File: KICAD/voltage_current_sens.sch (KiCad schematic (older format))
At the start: 17 parts, among them Q4 BC847, Q5 BC847, U8 LT6016, U9 AD8030

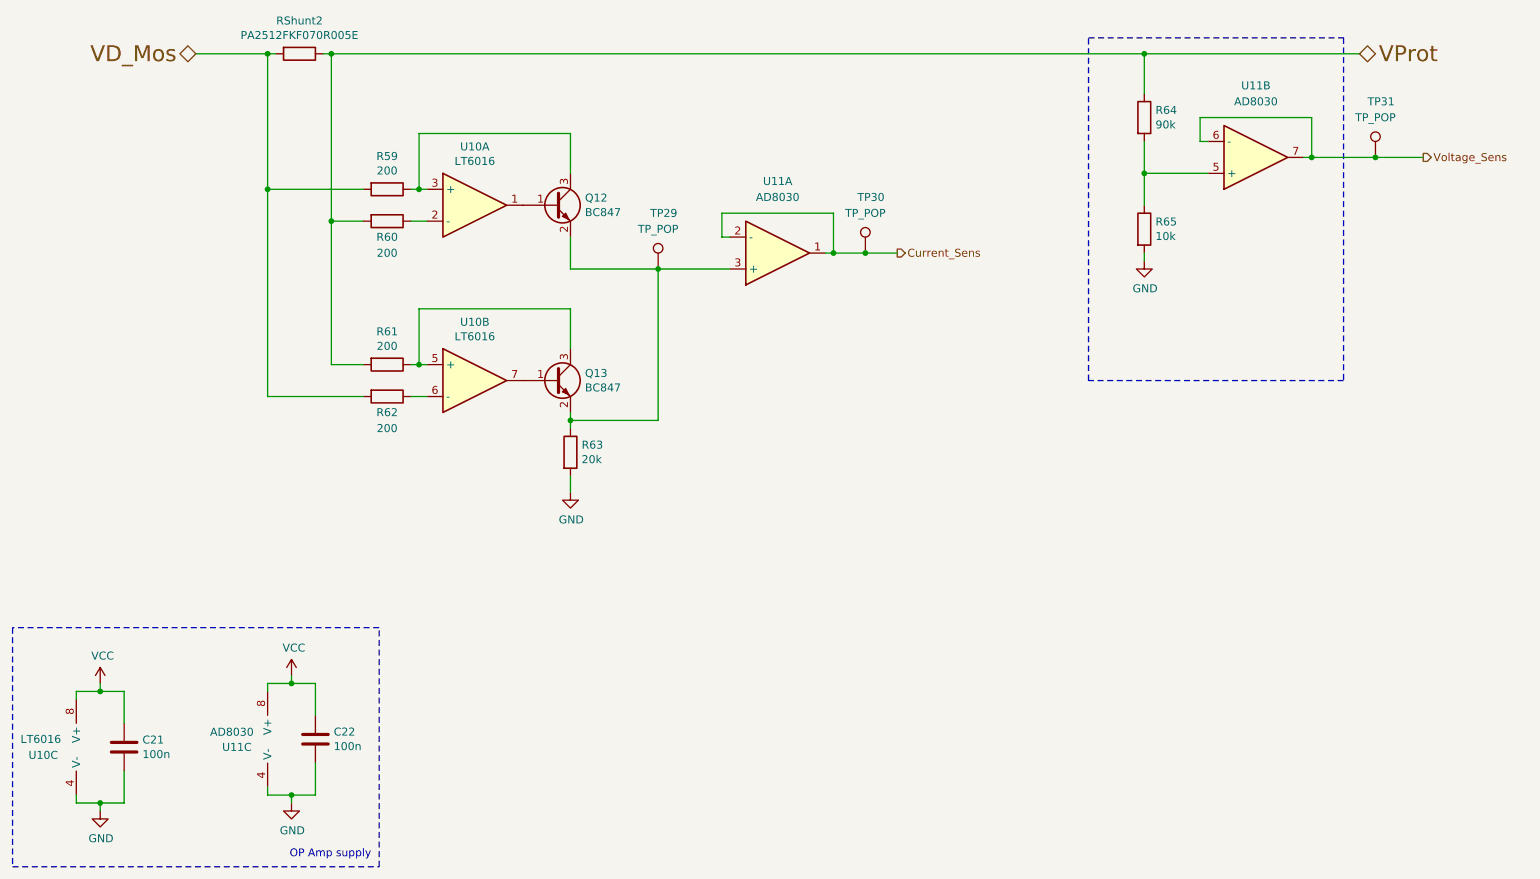
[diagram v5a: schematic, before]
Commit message: mod. ref rail on kicad
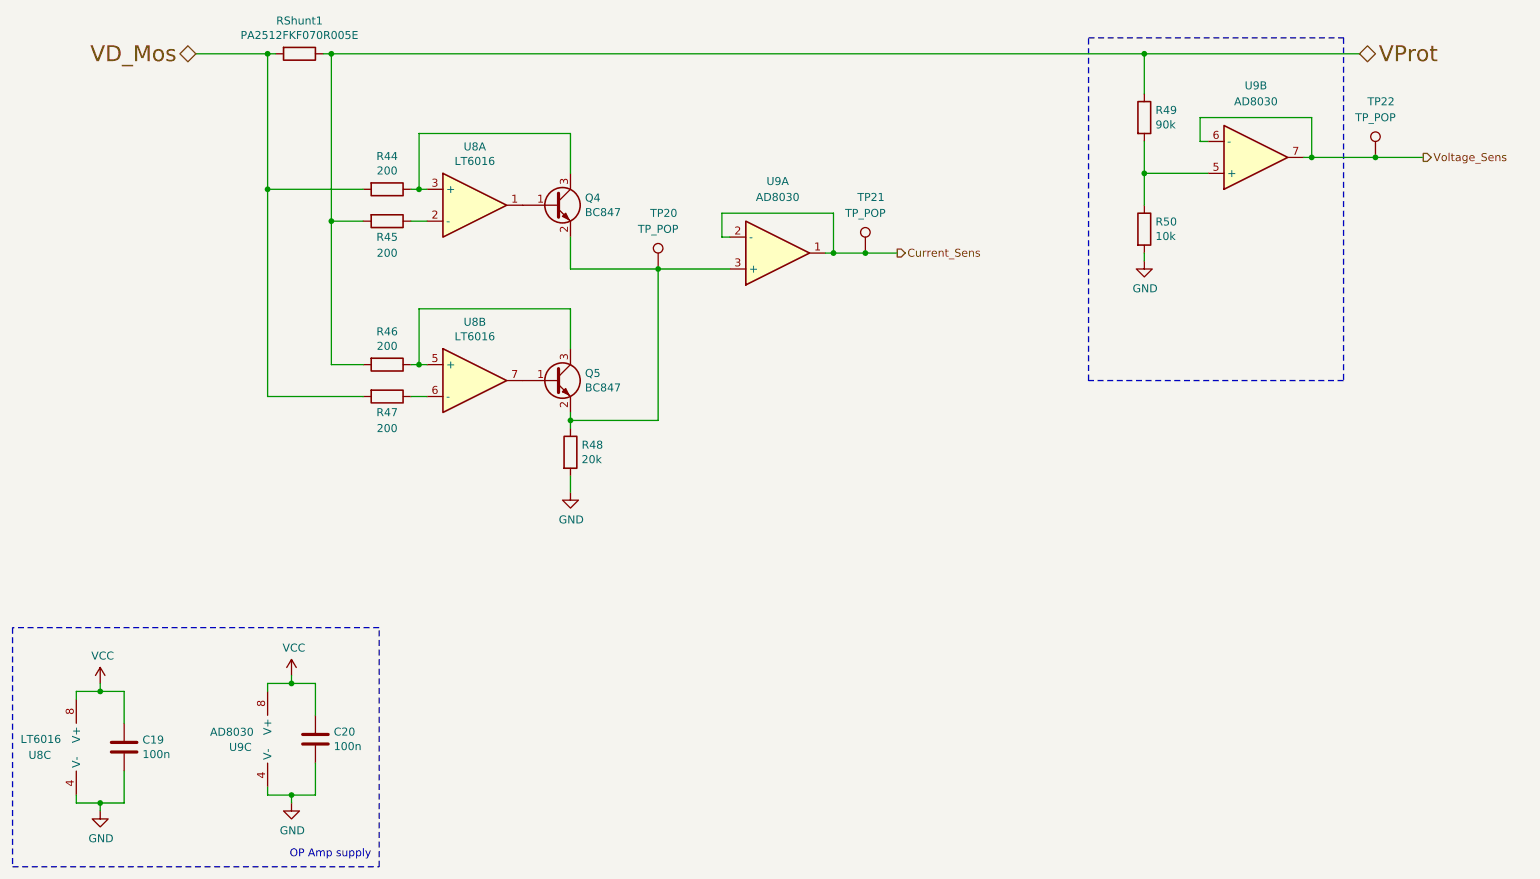
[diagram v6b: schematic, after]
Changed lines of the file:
@@
 AR Path="/60F19D5B/6109114F" Ref="RShunt2"  Part="1"
 AR Path="/60F171CE/6109114F" Ref="RShunt1"  Part="1"
-F 0 "RShunt2" V 2143 2600 50  0000 C CNN
+F 0 "RShunt1" V 2143 2600 50  0000 C CNN
 F 1 "PA2512FKF070R005E" V 2234 2600 50  0000 C CNN
 F 2 "Resistor_SMD:R_2512_6332Metric_Pad1.52x3.35mm_HandSolder" V 2280 2600 50  0001 C CNN
@@
 AR Path="/60F19D5B/61091B7C" Ref="R60"  Part="1"
 AR Path="/60F171CE/61091B7C" Ref="R45"  Part="1"
-F 0 "R60" V 3000 3650 50  0000 C CNN
+F 0 "R45" V 3000 3650 50  0000 C CNN
 F 1 "200" V 3100 3650 50  0000 C CNN
 F 2 "Sesame_footprint:R_0805_2012Metric_Pad1.20x1.40mm_HandSolder" V 2830 3650 50  0001 C CNN
@@
 AR Path="/60F19D5B/610923D6" Ref="R59"  Part="1"
 AR Path="/60F171CE/610923D6" Ref="R44"  Part="1"
-F 0 "R59" V 2693 3450 50  0000 C CNN
+F 0 "R44" V 2693 3450 50  0000 C CNN
 F 1 "200" V 2784 3450 50  0000 C CNN
 F 2 "Sesame_footprint:R_0805_2012Metric_Pad1.20x1.40mm_HandSolder" V 2830 3450 50  0001 C CNN
@@
 AR Path="/60F171CE/610DEA27" Ref="#PWR068"  Part="1"
 AR Path="/60F19D5B/610DEA27" Ref="#PWR080"  Part="1"
-F 0 "#PWR080" H 7650 3650 50  0001 C CNN
+F 0 "#PWR068" H 7650 3650 50  0001 C CNN
 F 1 "GND" H 7655 3727 50  0000 C CNN
 F 2 "" H 7650 3900 50  0001 C CNN
@@
 AR Path="/60F171CE/610DC636" Ref="R50"  Part="1"
 AR Path="/60F19D5B/610DC636" Ref="R65"  Part="1"
-F 0 "R65" H 7720 3746 50  0000 L CNN
+F 0 "R50" H 7720 3746 50  0000 L CNN
 F 1 "10k" H 7720 3655 50  0000 L CNN
 F 2 "Sesame_footprint:R_0805_2012Metric_Pad1.20x1.40mm_HandSolder" V 7580 3700 50  0001 C CNN
@@
 AR Path="/60F171CE/610DBB97" Ref="R49"  Part="1"
 AR Path="/60F19D5B/610DBB97" Ref="R64"  Part="1"
-F 0 "R64" H 7720 3046 50  0000 L CNN
+F 0 "R49" H 7720 3046 50  0000 L CNN
 F 1 "90k" H 7720 2955 50  0000 L CNN
 F 2 "Sesame_footprint:R_0805_2012Metric_Pad1.20x1.40mm_HandSolder" V 7580 3000 50  0001 C CNN
@@
 AR Path="/60F171CE/61382079" Ref="Q4"  Part="1"
 AR Path="/60F19D5B/61382079" Ref="Q12"  Part="1"
-F 0 "Q12" H 4141 3596 50  0000 L CNN
+F 0 "Q4" H 4141 3596 50  0000 L CNN
 F 1 "BC847" H 4141 3505 50  0000 L CNN
 F 2 "Package_TO_SOT_SMD:SOT-23" H 4150 3475 50  0001 L CIN
@@
 AR Path="/60F171CE/613844DA" Ref="Q5"  Part="1"
 AR Path="/60F19D5B/613844DA" Ref="Q13"  Part="1"
-F 0 "Q13" H 4141 4696 50  0000 L CNN
+F 0 "Q5" H 4141 4696 50  0000 L CNN
 F 1 "BC847" H 4141 4605 50  0000 L CNN
 F 2 "Package_TO_SOT_SMD:SOT-23" H 4150 4575 50  0001 L CIN
@@
 AR Path="/60F171CE/6138CEF9" Ref="R48"  Part="1"
 AR Path="/60F19D5B/6138CEF9" Ref="R63"  Part="1"
-F 0 "R63" H 4120 5146 50  0000 L CNN
+F 0 "R48" H 4120 5146 50  0000 L CNN
 F 1 "20k" H 4120 5055 50  0000 L CNN
 F 2 "Sesame_footprint:R_0805_2012Metric_Pad1.20x1.40mm_HandSolder" V 3980 5100 50  0001 C CNN
@@
 AR Path="/60F171CE/61391300" Ref="#PWR067"  Part="1"
 AR Path="/60F19D5B/61391300" Ref="#PWR079"  Part="1"
-F 0 "#PWR079" H 4050 5100 50  0001 C CNN
+F 0 "#PWR067" H 4050 5100 50  0001 C CNN
 F 1 "GND" H 4055 5177 50  0000 C CNN
 F 2 "" H 4050 5350 50  0001 C CNN
@@
 AR Path="/60F19D5B/61397C3C" Ref="R61"  Part="1"
 AR Path="/60F171CE/61397C3C" Ref="R46"  Part="1"
-F 0 "R61" V 2693 4550 50  0000 C CNN
+F 0 "R46" V 2693 4550 50  0000 C CNN
 F 1 "200" V 2784 4550 50  0000 C CNN
 F 2 "Sesame_footprint:R_0805_2012Metric_Pad1.20x1.40mm_HandSolder" V 2830 4550 50  0001 C CNN
@@
 AR Path="/60F19D5B/61398F33" Ref="R62"  Part="1"
 AR Path="/60F171CE/61398F33" Ref="R47"  Part="1"
-F 0 "R62" V 3000 4750 50  0000 C CNN
+F 0 "R47" V 3000 4750 50  0000 C CNN
 F 1 "200" V 3100 4750 50  0000 C CNN
 F 2 "Sesame_footprint:R_0805_2012Metric_Pad1.20x1.40mm_HandSolder" V 2830 4750 50  0001 C CNN
@@
 AR Path="/60F171CE/6139E98B" Ref="U9"  Part="2"
 AR Path="/60F19D5B/6139E98B" Ref="U11"  Part="2"
-F 0 "U11" H 8350 2800 50  0000 C CNN
+F 0 "U9" H 8350 2800 50  0000 C CNN
 F 1 "AD8030" H 8350 2900 50  0000 C CNN
 F 2 "Package_SO:SO-8_5.3x6.2mm_P1.27mm" H 8350 3250 50  0001 C CNN
@@
 AR Path="/60F171CE/613A5251" Ref="U9"  Part="1"
 AR Path="/60F19D5B/613A5251" Ref="U11"  Part="1"
-F 0 "U11" H 5350 3400 50  0000 C CNN
+F 0 "U9" H 5350 3400 50  0000 C CNN
 F 1 "AD8030" H 5350 3500 50  0000 C CNN
 F 2 "Package_SO:SO-8_5.3x6.2mm_P1.27mm" H 5350 3850 50  0001 C CNN
@@
 AR Path="/60F171CE/613B4715" Ref="C19"  Part="1"
 AR Path="/60F19D5B/613B4715" Ref="C21"  Part="1"
-F 0 "C21" H 1365 6996 50  0000 L CNN
+F 0 "C19" H 1365 6996 50  0000 L CNN
 F 1 "100n" H 1365 6905 50  0000 L CNN
 F 2 "Sesame_footprint:C_0805_2012Metric_Pad1.18x1.45mm_HandSolder" H 1288 6800 50  0001 C CNN
@@
 AR Path="/60F171CE/613B4720" Ref="#PWR064"  Part="1"
 AR Path="/60F19D5B/613B4720" Ref="#PWR076"  Part="1"
-F 0 "#PWR076" H 1100 7100 50  0001 C CNN
+F 0 "#PWR064" H 1100 7100 50  0001 C CNN
 F 1 "GND" H 1105 7177 50  0000 C CNN
 F 2 "" H 1100 7350 50  0001 C CNN
@@
 AR Path="/60F171CE/613B472D" Ref="#PWR063"  Part="1"
 AR Path="/60F19D5B/613B472D" Ref="#PWR075"  Part="1"
-F 0 "#PWR075" H 1100 6400 50  0001 C CNN
+F 0 "#PWR063" H 1100 6400 50  0001 C CNN
 F 1 "VCC" H 1115 6723 50  0000 C CNN
 F 2 "" H 1100 6550 50  0001 C CNN
@@
 AR Path="/60F171CE/613B7585" Ref="C20"  Part="1"
 AR Path="/60F19D5B/613B7585" Ref="C22"  Part="1"
-F 0 "C22" H 2565 6946 50  0000 L CNN
+F 0 "C20" H 2565 6946 50  0000 L CNN
 F 1 "100n" H 2565 6855 50  0000 L CNN
 F 2 "Sesame_footprint:C_0805_2012Metric_Pad1.18x1.45mm_HandSolder" H 2488 6750 50  0001 C CNN
@@
 AR Path="/60F171CE/613B7590" Ref="#PWR066"  Part="1"
 AR Path="/60F19D5B/613B7590" Ref="#PWR078"  Part="1"
-F 0 "#PWR078" H 2300 7050 50  0001 C CNN
+F 0 "#PWR066" H 2300 7050 50  0001 C CNN
 F 1 "GND" H 2305 7127 50  0000 C CNN
 F 2 "" H 2300 7300 50  0001 C CNN
@@
 AR Path="/60F171CE/613B759D" Ref="#PWR065"  Part="1"
 AR Path="/60F19D5B/613B759D" Ref="#PWR077"  Part="1"
-F 0 "#PWR077" H 2300 6350 50  0001 C CNN
+F 0 "#PWR065" H 2300 6350 50  0001 C CNN
 F 1 "VCC" H 2315 6673 50  0000 C CNN
 F 2 "" H 2300 6500 50  0001 C CNN
@@
 AR Path="/60F171CE/613B75A3" Ref="U9"  Part="3"
 AR Path="/60F19D5B/613B75A3" Ref="U11"  Part="3"
-F 0 "U11" H 2050 6850 50  0000 R CNN
+F 0 "U9" H 2050 6850 50  0000 R CNN
 F 1 "AD8030" H 2063 6945 50  0000 R CNN
 F 2 "Package_SO:SO-8_5.3x6.2mm_P1.27mm" H 2250 6900 50  0001 C CNN
@@
 AR Path="/60F171CE/615B8C9F" Ref="U8"  Part="1"
 AR Path="/60F19D5B/615B8C9F" Ref="U10"  Part="1"
-F 0 "U10" H 3450 3917 50  0000 C CNN
+F 0 "U8" H 3450 3917 50  0000 C CNN
 F 1 "LT6016" H 3450 3826 50  0000 C CNN
 F 2 "Package_SO:MSOP-8_3x3mm_P0.65mm" H 3450 3550 50  0001 C CNN
@@
 AR Path="/60F171CE/615BC62A" Ref="U8"  Part="2"
 AR Path="/60F19D5B/615BC62A" Ref="U10"  Part="2"
-F 0 "U10" H 3450 5017 50  0000 C CNN
+F 0 "U8" H 3450 5017 50  0000 C CNN
 F 1 "LT6016" H 3450 4926 50  0000 C CNN
 F 2 "Package_SO:MSOP-8_3x3mm_P0.65mm" H 3450 4650 50  0001 C CNN
@@
 AR Path="/60F171CE/615BFCFC" Ref="U8"  Part="3"
 AR Path="/60F19D5B/615BFCFC" Ref="U10"  Part="3"
-F 0 "U10" H 650 6900 50  0000 L CNN
+F 0 "U8" H 650 6900 50  0000 L CNN
 F 1 "LT6016" H 600 7000 50  0000 L CNN
 F 2 "Package_SO:MSOP-8_3x3mm_P0.65mm" H 1050 6950 50  0001 C CNN
@@
 AR Path="/60F171CE/6153C862" Ref="TP20"  Part="1"
 AR Path="/60F19D5B/6153C862" Ref="TP29"  Part="1"
-F 0 "TP29" H 4550 4300 50  0000 L CNN
+F 0 "TP20" H 4550 4300 50  0000 L CNN
 F 1 "TP_POP" H 4600 4200 50  0000 C CNN
 F 2 "TestPoint:TestPoint_Loop_D1.80mm_Drill1.0mm_Beaded" H 4800 3950 50  0001 C CNN
@@
 AR Path="/60F171CE/61544B27" Ref="TP22"  Part="1"
 AR Path="/60F19D5B/61544B27" Ref="TP31"  Part="1"
-F 0 "TP31" H 9050 3600 50  0000 L CNN
+F 0 "TP22" H 9050 3600 50  0000 L CNN
 F 1 "TP_POP" H 9100 3500 50  0000 C CNN
 F 2 "TestPoint:TestPoint_Loop_D1.80mm_Drill1.0mm_Beaded" H 9300 3250 50  0001 C CNN
@@
 AR Path="/60F171CE/6154A16C" Ref="TP21"  Part="1"
 AR Path="/60F19D5B/6154A16C" Ref="TP30"  Part="1"
-F 0 "TP30" H 5850 4200 50  0000 L CNN
+F 0 "TP21" H 5850 4200 50  0000 L CNN
 F 1 "TP_POP" H 5900 4100 50  0000 C CNN
 F 2 "TestPoint:TestPoint_Loop_D1.80mm_Drill1.0mm_Beaded" H 6100 3850 50  0001 C CNN

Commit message: cleanup silkscreen
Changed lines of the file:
@@
 $Descr A4 11693 8268
 encoding utf-8
-Sheet 8 17
+Sheet 11 17
 Title "SESAME"
 Date ""
@@
 AR Path="/60F19D5B/6109114F" Ref="RShunt2"  Part="1"
 AR Path="/60F171CE/6109114F" Ref="RShunt1"  Part="1"
-F 0 "RShunt1" V 2143 2600 50  0000 C CNN
+F 0 "RShunt2" V 2143 2600 50  0000 C CNN
 F 1 "PA2512FKF070R005E" V 2234 2600 50  0000 C CNN
 F 2 "Resistor_SMD:R_2512_6332Metric_Pad1.52x3.35mm_HandSolder" V 2280 2600 50  0001 C CNN
@@
 AR Path="/60F19D5B/61091B7C" Ref="R60"  Part="1"
 AR Path="/60F171CE/61091B7C" Ref="R45"  Part="1"
-F 0 "R45" V 3000 3650 50  0000 C CNN
+F 0 "R60" V 3000 3650 50  0000 C CNN
 F 1 "200" V 3100 3650 50  0000 C CNN
 F 2 "Sesame_footprint:R_0805_2012Metric_Pad1.20x1.40mm_HandSolder" V 2830 3650 50  0001 C CNN
@@
 AR Path="/60F19D5B/610923D6" Ref="R59"  Part="1"
 AR Path="/60F171CE/610923D6" Ref="R44"  Part="1"
-F 0 "R44" V 2693 3450 50  0000 C CNN
+F 0 "R59" V 2693 3450 50  0000 C CNN
 F 1 "200" V 2784 3450 50  0000 C CNN
 F 2 "Sesame_footprint:R_0805_2012Metric_Pad1.20x1.40mm_HandSolder" V 2830 3450 50  0001 C CNN
@@
 AR Path="/60F171CE/610DEA27" Ref="#PWR068"  Part="1"
 AR Path="/60F19D5B/610DEA27" Ref="#PWR080"  Part="1"
-F 0 "#PWR068" H 7650 3650 50  0001 C CNN
+F 0 "#PWR080" H 7650 3650 50  0001 C CNN
 F 1 "GND" H 7655 3727 50  0000 C CNN
 F 2 "" H 7650 3900 50  0001 C CNN
@@
 AR Path="/60F171CE/610DC636" Ref="R50"  Part="1"
 AR Path="/60F19D5B/610DC636" Ref="R65"  Part="1"
-F 0 "R50" H 7720 3746 50  0000 L CNN
+F 0 "R65" H 7720 3746 50  0000 L CNN
 F 1 "10k" H 7720 3655 50  0000 L CNN
 F 2 "Sesame_footprint:R_0805_2012Metric_Pad1.20x1.40mm_HandSolder" V 7580 3700 50  0001 C CNN
@@
 AR Path="/60F171CE/610DBB97" Ref="R49"  Part="1"
 AR Path="/60F19D5B/610DBB97" Ref="R64"  Part="1"
-F 0 "R49" H 7720 3046 50  0000 L CNN
+F 0 "R64" H 7720 3046 50  0000 L CNN
 F 1 "90k" H 7720 2955 50  0000 L CNN
 F 2 "Sesame_footprint:R_0805_2012Metric_Pad1.20x1.40mm_HandSolder" V 7580 3000 50  0001 C CNN
@@
 AR Path="/60F171CE/61382079" Ref="Q4"  Part="1"
 AR Path="/60F19D5B/61382079" Ref="Q12"  Part="1"
-F 0 "Q4" H 4141 3596 50  0000 L CNN
+F 0 "Q12" H 4141 3596 50  0000 L CNN
 F 1 "BC847" H 4141 3505 50  0000 L CNN
 F 2 "Package_TO_SOT_SMD:SOT-23" H 4150 3475 50  0001 L CIN
@@
 AR Path="/60F171CE/613844DA" Ref="Q5"  Part="1"
 AR Path="/60F19D5B/613844DA" Ref="Q13"  Part="1"
-F 0 "Q5" H 4141 4696 50  0000 L CNN
+F 0 "Q13" H 4141 4696 50  0000 L CNN
 F 1 "BC847" H 4141 4605 50  0000 L CNN
 F 2 "Package_TO_SOT_SMD:SOT-23" H 4150 4575 50  0001 L CIN
@@
 AR Path="/60F171CE/6138CEF9" Ref="R48"  Part="1"
 AR Path="/60F19D5B/6138CEF9" Ref="R63"  Part="1"
-F 0 "R48" H 4120 5146 50  0000 L CNN
+F 0 "R63" H 4120 5146 50  0000 L CNN
 F 1 "20k" H 4120 5055 50  0000 L CNN
 F 2 "Sesame_footprint:R_0805_2012Metric_Pad1.20x1.40mm_HandSolder" V 3980 5100 50  0001 C CNN
@@
 AR Path="/60F171CE/61391300" Ref="#PWR067"  Part="1"
 AR Path="/60F19D5B/61391300" Ref="#PWR079"  Part="1"
-F 0 "#PWR067" H 4050 5100 50  0001 C CNN
+F 0 "#PWR079" H 4050 5100 50  0001 C CNN
 F 1 "GND" H 4055 5177 50  0000 C CNN
 F 2 "" H 4050 5350 50  0001 C CNN
@@
 AR Path="/60F19D5B/61397C3C" Ref="R61"  Part="1"
 AR Path="/60F171CE/61397C3C" Ref="R46"  Part="1"
-F 0 "R46" V 2693 4550 50  0000 C CNN
+F 0 "R61" V 2693 4550 50  0000 C CNN
 F 1 "200" V 2784 4550 50  0000 C CNN
 F 2 "Sesame_footprint:R_0805_2012Metric_Pad1.20x1.40mm_HandSolder" V 2830 4550 50  0001 C CNN
@@
 AR Path="/60F19D5B/61398F33" Ref="R62"  Part="1"
 AR Path="/60F171CE/61398F33" Ref="R47"  Part="1"
-F 0 "R47" V 3000 4750 50  0000 C CNN
+F 0 "R62" V 3000 4750 50  0000 C CNN
 F 1 "200" V 3100 4750 50  0000 C CNN
 F 2 "Sesame_footprint:R_0805_2012Metric_Pad1.20x1.40mm_HandSolder" V 2830 4750 50  0001 C CNN
@@
 AR Path="/60F171CE/6139E98B" Ref="U9"  Part="2"
 AR Path="/60F19D5B/6139E98B" Ref="U11"  Part="2"
-F 0 "U9" H 8350 2800 50  0000 C CNN
+F 0 "U11" H 8350 2800 50  0000 C CNN
 F 1 "AD8030" H 8350 2900 50  0000 C CNN
 F 2 "Package_SO:SO-8_5.3x6.2mm_P1.27mm" H 8350 3250 50  0001 C CNN
@@
 AR Path="/60F171CE/613A5251" Ref="U9"  Part="1"
 AR Path="/60F19D5B/613A5251" Ref="U11"  Part="1"
-F 0 "U9" H 5350 3400 50  0000 C CNN
+F 0 "U11" H 5350 3400 50  0000 C CNN
 F 1 "AD8030" H 5350 3500 50  0000 C CNN
 F 2 "Package_SO:SO-8_5.3x6.2mm_P1.27mm" H 5350 3850 50  0001 C CNN
@@
 AR Path="/60F171CE/613B4715" Ref="C19"  Part="1"
 AR Path="/60F19D5B/613B4715" Ref="C21"  Part="1"
-F 0 "C19" H 1365 6996 50  0000 L CNN
+F 0 "C21" H 1365 6996 50  0000 L CNN
 F 1 "100n" H 1365 6905 50  0000 L CNN
 F 2 "Sesame_footprint:C_0805_2012Metric_Pad1.18x1.45mm_HandSolder" H 1288 6800 50  0001 C CNN
@@
 AR Path="/60F171CE/613B4720" Ref="#PWR064"  Part="1"
 AR Path="/60F19D5B/613B4720" Ref="#PWR076"  Part="1"
-F 0 "#PWR064" H 1100 7100 50  0001 C CNN
+F 0 "#PWR076" H 1100 7100 50  0001 C CNN
 F 1 "GND" H 1105 7177 50  0000 C CNN
 F 2 "" H 1100 7350 50  0001 C CNN
@@
 AR Path="/60F171CE/613B472D" Ref="#PWR063"  Part="1"
 AR Path="/60F19D5B/613B472D" Ref="#PWR075"  Part="1"
-F 0 "#PWR063" H 1100 6400 50  0001 C CNN
+F 0 "#PWR075" H 1100 6400 50  0001 C CNN
 F 1 "VCC" H 1115 6723 50  0000 C CNN
 F 2 "" H 1100 6550 50  0001 C CNN
@@
 AR Path="/60F171CE/613B7585" Ref="C20"  Part="1"
 AR Path="/60F19D5B/613B7585" Ref="C22"  Part="1"
-F 0 "C20" H 2565 6946 50  0000 L CNN
+F 0 "C22" H 2565 6946 50  0000 L CNN
 F 1 "100n" H 2565 6855 50  0000 L CNN
 F 2 "Sesame_footprint:C_0805_2012Metric_Pad1.18x1.45mm_HandSolder" H 2488 6750 50  0001 C CNN
@@
 AR Path="/60F171CE/613B7590" Ref="#PWR066"  Part="1"
 AR Path="/60F19D5B/613B7590" Ref="#PWR078"  Part="1"
-F 0 "#PWR066" H 2300 7050 50  0001 C CNN
+F 0 "#PWR078" H 2300 7050 50  0001 C CNN
 F 1 "GND" H 2305 7127 50  0000 C CNN
 F 2 "" H 2300 7300 50  0001 C CNN
@@
 AR Path="/60F171CE/613B759D" Ref="#PWR065"  Part="1"
 AR Path="/60F19D5B/613B759D" Ref="#PWR077"  Part="1"
-F 0 "#PWR065" H 2300 6350 50  0001 C CNN
+F 0 "#PWR077" H 2300 6350 50  0001 C CNN
 F 1 "VCC" H 2315 6673 50  0000 C CNN
 F 2 "" H 2300 6500 50  0001 C CNN
@@
 AR Path="/60F171CE/613B75A3" Ref="U9"  Part="3"
 AR Path="/60F19D5B/613B75A3" Ref="U11"  Part="3"
-F 0 "U9" H 2050 6850 50  0000 R CNN
+F 0 "U11" H 2050 6850 50  0000 R CNN
 F 1 "AD8030" H 2063 6945 50  0000 R CNN
 F 2 "Package_SO:SO-8_5.3x6.2mm_P1.27mm" H 2250 6900 50  0001 C CNN
@@
 AR Path="/60F171CE/615B8C9F" Ref="U8"  Part="1"
 AR Path="/60F19D5B/615B8C9F" Ref="U10"  Part="1"
-F 0 "U8" H 3450 3917 50  0000 C CNN
+F 0 "U10" H 3450 3917 50  0000 C CNN
 F 1 "LT6016" H 3450 3826 50  0000 C CNN
 F 2 "Package_SO:MSOP-8_3x3mm_P0.65mm" H 3450 3550 50  0001 C CNN
@@
 AR Path="/60F171CE/615BC62A" Ref="U8"  Part="2"
 AR Path="/60F19D5B/615BC62A" Ref="U10"  Part="2"
-F 0 "U8" H 3450 5017 50  0000 C CNN
+F 0 "U10" H 3450 5017 50  0000 C CNN
 F 1 "LT6016" H 3450 4926 50  0000 C CNN
 F 2 "Package_SO:MSOP-8_3x3mm_P0.65mm" H 3450 4650 50  0001 C CNN
@@
 AR Path="/60F171CE/615BFCFC" Ref="U8"  Part="3"
 AR Path="/60F19D5B/615BFCFC" Ref="U10"  Part="3"
-F 0 "U8" H 650 6900 50  0000 L CNN
+F 0 "U10" H 650 6900 50  0000 L CNN
 F 1 "LT6016" H 600 7000 50  0000 L CNN
 F 2 "Package_SO:MSOP-8_3x3mm_P0.65mm" H 1050 6950 50  0001 C CNN
@@
 AR Path="/60F171CE/6153C862" Ref="TP20"  Part="1"
 AR Path="/60F19D5B/6153C862" Ref="TP29"  Part="1"
-F 0 "TP20" H 4550 4300 50  0000 L CNN
+F 0 "TP29" H 4550 4300 50  0000 L CNN
 F 1 "TP_POP" H 4600 4200 50  0000 C CNN
 F 2 "TestPoint:TestPoint_Loop_D1.80mm_Drill1.0mm_Beaded" H 4800 3950 50  0001 C CNN
@@
 AR Path="/60F171CE/61544B27" Ref="TP22"  Part="1"
 AR Path="/60F19D5B/61544B27" Ref="TP31"  Part="1"
-F 0 "TP22" H 9050 3600 50  0000 L CNN
+F 0 "TP31" H 9050 3600 50  0000 L CNN
 F 1 "TP_POP" H 9100 3500 50  0000 C CNN
 F 2 "TestPoint:TestPoint_Loop_D1.80mm_Drill1.0mm_Beaded" H 9300 3250 50  0001 C CNN
@@
 AR Path="/60F171CE/6154A16C" Ref="TP21"  Part="1"
 AR Path="/60F19D5B/6154A16C" Ref="TP30"  Part="1"
-F 0 "TP21" H 5850 4200 50  0000 L CNN
+F 0 "TP30" H 5850 4200 50  0000 L CNN
 F 1 "TP_POP" H 5900 4100 50  0000 C CNN
 F 2 "TestPoint:TestPoint_Loop_D1.80mm_Drill1.0mm_Beaded" H 6100 3850 50  0001 C CNN
